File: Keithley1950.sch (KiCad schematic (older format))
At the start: 92 parts, among them J1 Conn_01x14, J2 Conn_01x03, J3 Conn_01x02, K1 Relay_SP2P, K2 Relay_SP2P, K3 Relay_SP3P, K4 Relay_SP2P, K5 Relay_SP2P, K6 Relay_SP3P, K7 Relay_SP3P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

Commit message: Fixes, tweaks, tag rev A
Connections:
- net -15V: now also U2.12 (V-)
- net GNDA: no longer U2.12 (V-)
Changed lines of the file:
@@
 Wire Wire Line
 	8400 2600 8600 2600
-$Comp
-L power:GNDA #PWR021
-U 1 1 5D0D8129
-P 7600 3100
-F 0 "#PWR021" H 7600 2850 50  0001 C CNN
-F 1 "GNDA" H 7605 2927 50  0000 C CNN
-F 2 "" H 7600 3100 50  0001 C CNN
-F 3 "" H 7600 3100 50  0001 C CNN
-	1    7600 3100
-	1    0    0    -1
-$EndComp
 Wire Wire Line
 	1400 3600 1400 3100
@@
 	1    0    0    -1
 $EndComp
+$Comp
+L project:-15V #PWR?
+U 1 1 5D20A15B
+P 7600 3100
+F 0 "#PWR?" H 7600 3200 50  0001 C CNN
+F 1 "-15V" H 7615 3273 50  0000 C CNN
+F 2 "" H 7600 3100 50  0001 C CNN
+F 3 "" H 7600 3100 50  0001 C CNN
+	1    7600 3100
+	-1   0    0    1
+$EndComp
 $EndSCHEMATC

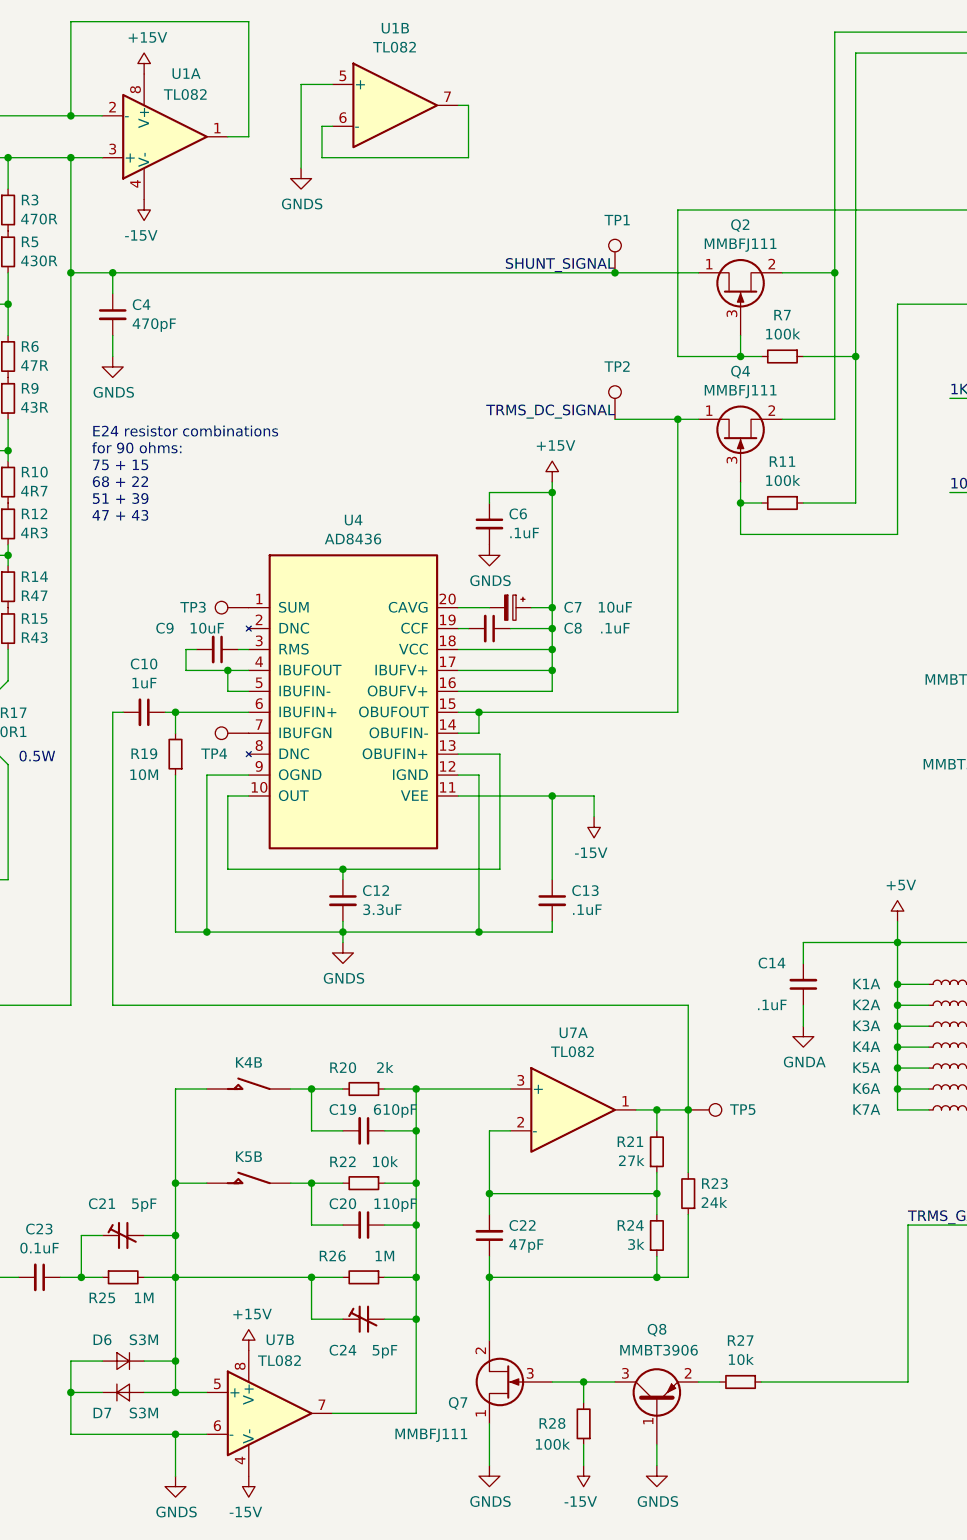
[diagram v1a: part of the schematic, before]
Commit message: Revision B
1. Clearance for high voltage lines
2. 14 pin connector courtyard overlap
3. 24K resistor is DNP
4. Fix swapped inputs of U7B
5. Change c7 to tantalum type Bx
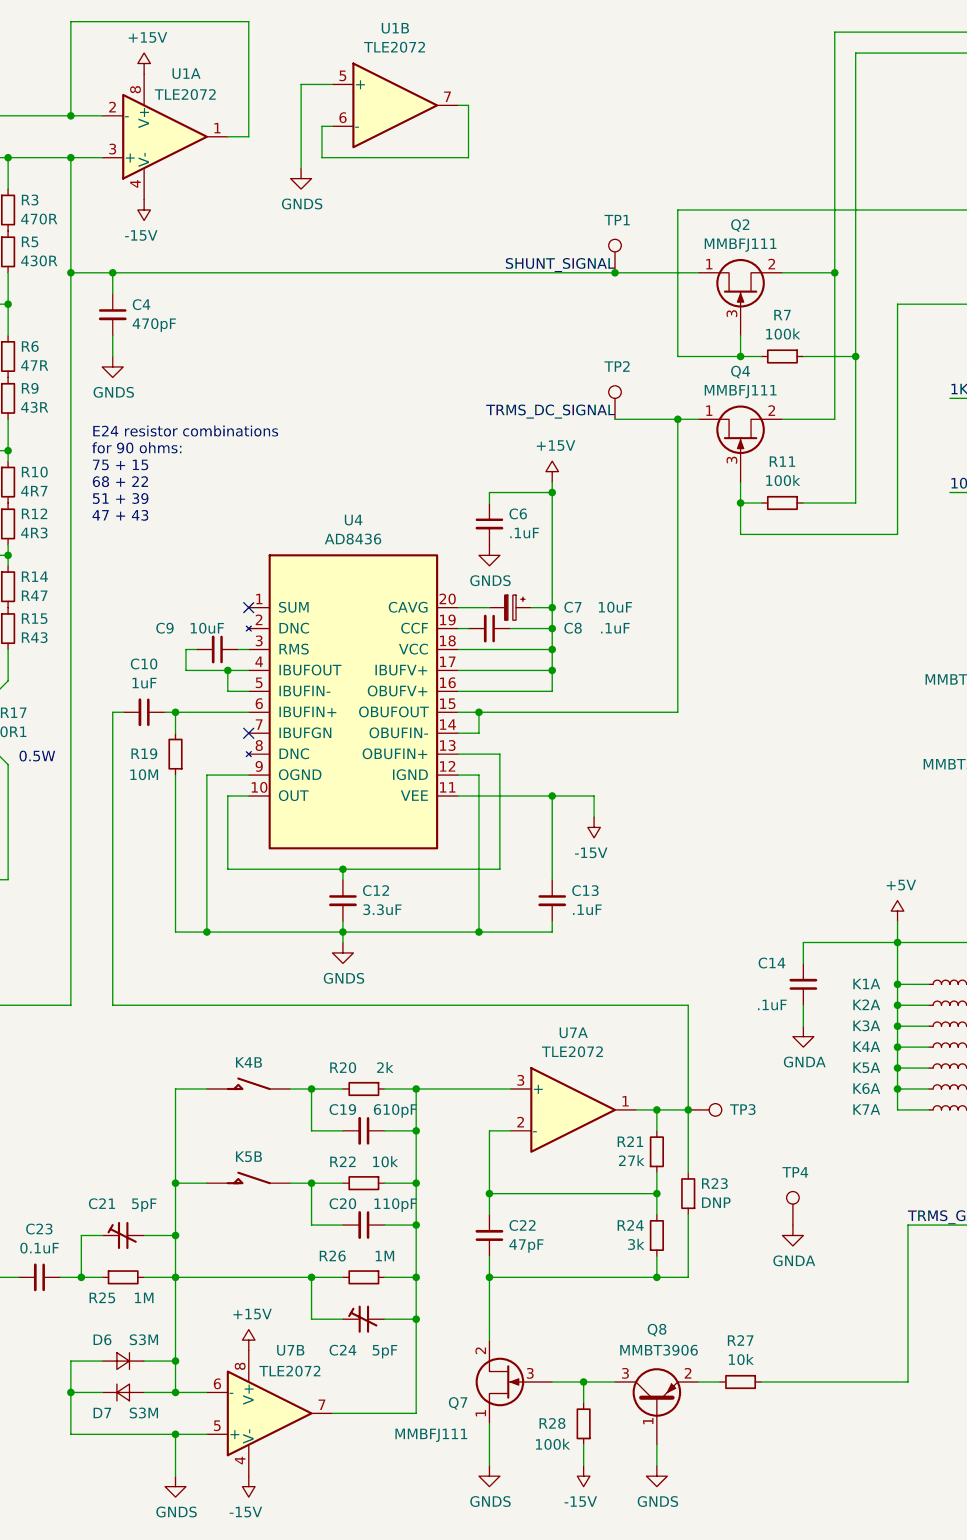
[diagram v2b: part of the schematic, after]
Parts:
- removed TP3: TestPoint, TestPoint:TestPoint_Pad_D2.5mm, symbol Connector:TestPoint
- C7: footprint Capacitor_SMD:CP_Elec_5x5.4 -> Capacitor_Tantalum_SMD:CP_EIA-3528-21_Kemet-B
- R23: value 24k -> DNP
- TP4: footprint TestPoint:TestPoint_Pad_D2.5mm -> TestPoint:TestPoint_THTPad_D1.5mm_Drill0.7mm
- U1, U7: value TL082 -> TLE2072
- renumbered TP5 to TP3
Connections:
- net GNDA: now also TP4.1, U7.5 (+); no longer U7.6 (-)
- net at C21.2, C24.1, D6.1 (K)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: now also U7.6 (-); no longer U7.5 (+)
- net at U4.7 (IBUFGN): no longer TP4.1
- no-connect marks 10 -> 12
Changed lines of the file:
@@
 EESchema Schematic File Version 4
 LIBS:Keithley1950-cache
-EELAYER 29 0
+EELAYER 30 0
 EELAYER END
 $Descr A4 11693 8268
@@
 Sheet 1 1
 Title "Keithley DMM Option 1950"
-Date "2019-06-23"
-Rev "A"
+Date "2019-11-16"
+Rev "B"
 Comp "OpenScopeProject"
 Comment1 "AC TRMS Volts and AC/DC AMPS board"
@@
 	6150 4950 6150 5050
 $Comp
-L power:GNDA #PWR033
+L power:GNDA #PWR032
 U 1 1 5CF73799
 P 6150 5350
-F 0 "#PWR033" H 6150 5100 50  0001 C CNN
+F 0 "#PWR032" H 6150 5100 50  0001 C CNN
 F 1 "GNDA" H 6155 5177 50  0000 C CNN
 F 2 "" H 6150 5350 50  0001 C CNN
@@
 Connection ~ 1100 5750
 $Comp
-L power:GNDS #PWR032
+L power:GNDS #PWR033
 U 1 1 5D2CCBAF
 P 1550 5450
-F 0 "#PWR032" H 1550 5200 50  0001 C CNN
+F 0 "#PWR033" H 1550 5200 50  0001 C CNN
 F 1 "GNDS" H 1555 5277 50  0000 C CNN
 F 2 "" H 1550 5450 50  0001 C CNN
@@
 P 5050 5750
 F 0 "U7" H 5050 6117 50  0000 C CNN
-F 1 "TL082" H 5050 6026 50  0000 C CNN
+F 1 "TLE2072" H 5050 6026 50  0000 C CNN
 F 2 "Package_SO:SOIC-8_3.9x4.9mm_P1.27mm" H 5050 5750 50  0001 C CNN
 F 3 "http://www.ti.com/lit/ds/symlink/tl081.pdf" H 5050 5750 50  0001 C CNN
@@
 U 2 1 5CB57F9E
 P 3600 7200
-F 0 "U7" H 3650 7550 50  0000 C CNN
-F 1 "TL082" H 3650 7450 50  0000 C CNN
+F 0 "U7" H 3700 6900 50  0000 C CNN
+F 1 "TLE2072" H 3700 7000 50  0000 C CNN
 F 2 "Package_SO:SOIC-8_3.9x4.9mm_P1.27mm" H 3600 7200 50  0001 C CNN
 F 3 "http://www.ti.com/lit/ds/symlink/tl081.pdf" H 3600 7200 50  0001 C CNN
 	2    3600 7200
-	1    0    0    -1
+	1    0    0    1
 $EndComp
 $Comp
@@
 P 3600 7200
 F 0 "U7" H 3558 7246 50  0001 L CNN
-F 1 "TL082" H 3558 7155 50  0001 L CNN
+F 1 "TLE2072" H 3558 7155 50  0001 L CNN
 F 2 "Package_SO:SOIC-8_3.9x4.9mm_P1.27mm" H 3600 7200 50  0001 C CNN
 F 3 "http://www.ti.com/lit/ds/symlink/tl081.pdf" H 3600 7200 50  0001 C CNN
@@
 P 3100 1100
 F 0 "U1" H 3200 800 50  0000 C CNN
-F 1 "TL082" H 3200 900 50  0000 C CNN
+F 1 "TLE2072" H 3200 900 50  0000 C CNN
 F 2 "Package_SO:SOIC-8_3.9x4.9mm_P1.27mm" H 3100 1100 50  0001 C CNN
 F 3 "http://www.ti.com/lit/ds/symlink/tl081.pdf" H 3100 1100 50  0001 C CNN
@@
 P 4200 950
 F 0 "U1" H 4200 1317 50  0000 C CNN
-F 1 "TL082" H 4200 1226 50  0000 C CNN
+F 1 "TLE2072" H 4200 1226 50  0000 C CNN
 F 2 "Package_SO:SOIC-8_3.9x4.9mm_P1.27mm" H 4200 950 50  0001 C CNN
 F 3 "http://www.ti.com/lit/ds/symlink/tl081.pdf" H 4200 950 50  0001 C CNN
@@
 P 3100 1100
 F 0 "U1" H 3058 1146 50  0001 L CNN
-F 1 "TL082" H 3058 1055 50  0001 L CNN
+F 1 "TLE2072" H 3058 1055 50  0001 L CNN
 F 2 "Package_SO:SOIC-8_3.9x4.9mm_P1.27mm" H 3100 1100 50  0001 C CNN
 F 3 "http://www.ti.com/lit/ds/symlink/tl081.pdf" H 3100 1100 50  0001 C CNN
@@
 P 5600 6150
 F 0 "R23" H 5541 6104 50  0000 R CNN
-F 1 "24k" H 5541 6195 50  0000 R CNN
+F 1 "DNP" H 5541 6195 50  0000 R CNN
 F 2 "Resistor_SMD:R_0805_2012Metric" H 5600 6150 50  0001 C CNN
 F 3 "~" H 5600 6150 50  0001 C CNN
@@
 $EndComp
 $Comp
-L Connector:TestPoint TP5
+L Connector:TestPoint TP3
 U 1 1 5DD359C9
 P 5600 5750
-F 0 "TP5" V 5600 5950 50  0000 L CNN
+F 0 "TP3" V 5600 5950 50  0000 L CNN
 F 1 "TestPoint" V 5500 5950 50  0001 L CNN
 F 2 "TestPoint:TestPoint_Pad_D2.5mm" H 5800 5750 50  0001 C CNN
@@
 $EndComp
 $Comp
-L Connector:TestPoint TP3
-U 1 1 5D353FB4
-P 3500 3350
-F 0 "TP3" V 3500 3550 50  0000 L CNN
-F 1 "TestPoint" H 3100 3500 50  0001 L CNN
-F 2 "TestPoint:TestPoint_Pad_D2.5mm" H 3700 3350 50  0001 C CNN
-F 3 "~" H 3700 3350 50  0001 C CNN
-	1    3500 3350
-	0    -1   -1   0
-$EndComp
-$Comp
 L Device:C_Small C13
 U 1 1 5D3760C8
@@
 F 0 "C7" V 4750 3650 50  0000 C CNN
 F 1 "10uF" V 4750 3850 50  0000 C CNN
-F 2 "Capacitor_SMD:CP_Elec_5x5.4" H 4750 3350 50  0001 C CNN
+F 2 "Capacitor_Tantalum_SMD:CP_EIA-3528-21_Kemet-B" H 4750 3350 50  0001 C CNN
 F 3 "~" H 4750 3350 50  0001 C CNN
 	1    4750 3350
@@
 $EndComp
 $Comp
-L Connector:TestPoint TP4
-U 1 1 5DE74621
-P 3500 3950
-F 0 "TP4" V 3400 4050 50  0000 L CNN
-F 1 "TestPoint" H 3100 4100 50  0001 L CNN
-F 2 "TestPoint:TestPoint_Pad_D2.5mm" H 3700 3950 50  0001 C CNN
-F 3 "~" H 3700 3950 50  0001 C CNN
-	1    3500 3950
-	0    -1   -1   0
-$EndComp
-$Comp
 L Device:C_Small C12
 U 1 1 5E0E7EB6
@@
 $EndComp
 $Comp
-L project:-15V #PWR?
+L project:-15V #PWR021
 U 1 1 5D20A15B
 P 7600 3100
-F 0 "#PWR?" H 7600 3200 50  0001 C CNN
+F 0 "#PWR021" H 7600 3200 50  0001 C CNN
 F 1 "-15V" H 7615 3273 50  0000 C CNN
 F 2 "" H 7600 3100 50  0001 C CNN
@@
 	-1   0    0    1
 $EndComp
+NoConn ~ 3500 3950
+NoConn ~ 3500 3350
+$Comp
+L Connector:TestPoint TP4
+U 1 1 5DF7CDFA
+P 6100 6300
+F 0 "TP4" H 6050 6550 50  0000 L CNN
+F 1 "TestPoint" V 6000 6500 50  0001 L CNN
+F 2 "TestPoint:TestPoint_THTPad_D1.5mm_Drill0.7mm" H 6300 6300 50  0001 C CNN
+F 3 "~" H 6300 6300 50  0001 C CNN
+	1    6100 6300
+	1    0    0    -1
+$EndComp
+$Comp
+L power:GNDA #PWR0101
+U 1 1 5DF7D597
+P 6100 6300
+F 0 "#PWR0101" H 6100 6050 50  0001 C CNN
+F 1 "GNDA" H 6105 6127 50  0000 C CNN
+F 2 "" H 6100 6300 50  0001 C CNN
+F 3 "" H 6100 6300 50  0001 C CNN
+	1    6100 6300
+	1    0    0    -1
+$EndComp
 $EndSCHEMATC
